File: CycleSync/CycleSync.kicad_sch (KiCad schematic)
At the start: 0 parts

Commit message: M1.1: hierarchical sheet skeleton + net-map topology (6 sheets, all interface labels placed/imported)
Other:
- added sheet Audio_ADC (Audio_ADC.kicad_sch)
- added sheet Audio_DAC (Audio_DAC.kicad_sch)
- added sheet GNSS_RF (GNSS_RF.kicad_sch)
- added sheet MCU (MCU.kicad_sch)
- added sheet Power (Power.kicad_sch)
- added sheet USB_PD (USB_PD.kicad_sch)

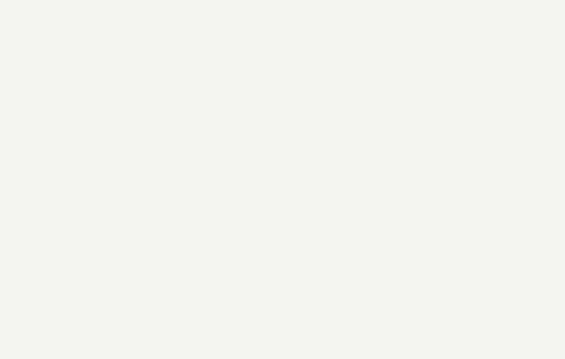
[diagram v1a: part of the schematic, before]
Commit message: M1.2: MCU core supply, fixed-function pins, GPIO0-8 assignment
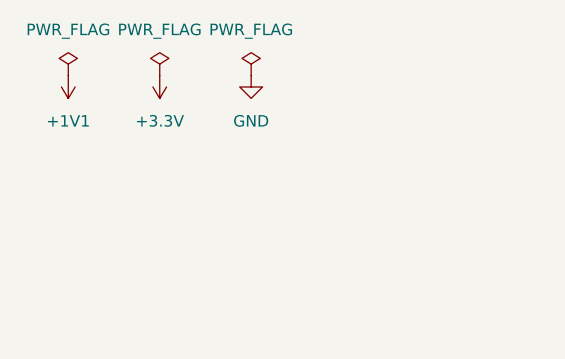
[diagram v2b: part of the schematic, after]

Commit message: finishing Phase 1.5
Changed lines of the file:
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@@
 			)
 		)
-		(pin "I2C_SCL" input
+		(pin "I2C_SCL" bidirectional
 			(at 81.6293 100.33 90)
 			(effects

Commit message: s
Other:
- added sheet Daughter_IO (Daughter_IO.kicad_sch)
- sheet Audio_ADC ports: added LINE_IN_L, LINE_IN_R; removed none
- sheet Audio_DAC ports: added LINE_OUT_L, LINE_OUT_R; removed none
- sheet GNSS_RF ports: added GNSS_BCKP_CUTOFF, GNSS_FIX_STATUS, GNSS_RESET_N; removed none
- sheet MCU ports: added GNSS_BCKP_CUTOFF, GNSS_FIX_LED, GNSS_FIX_STATUS, GNSS_RESET_N, GNSS_VCC_CUTOFF, PD_IRQ, USB_D_N, USB_D_P; removed USB_DM, USB_DP
- sheet Power ports: added GNSS_VCC_CUTOFF, PP5V, VBUS_HOST_5V, VBUS_PD_5V; removed none
- sheet USB_PD ports: added CC1, CC2, PDIN_CC1, PDIN_CC2, PD_IRQ, PP5V, PPHV, VBUS; removed USB_DM, USB_DP
- note added: "CYCLESYNC ASSEMBLY VARIANTS 1. PD + LINE-IN: PD_OPTION + LINE_IN_OPTION 2. PD + PLAYBACK-ONLY: PD_OPTION 3. NO-PD + LINE-IN: NO_PD_OPTION + LINE_IN_OPTION 4. NO-PD + PLAYBACK-ONLY: NO_PD_OPTION COMPONENTS WITH A BLANK VARIANT FIELD ARE COMMON TO ALL BUILDS UNLESS MARKED DNP."
- title: (none) -> CYCLESYNC SYSTEM SCHEMATIC

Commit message: verified schematic wirings
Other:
- sheet USB_PD ports: added VBUS_PD_5V; removed PPHV
- note added: "ASSEMBLY VARIANTS 1. PD + LINE-IN: PD_OPTION + LINE_IN_OPTION 2. PD + PLAYBACK: PD_OPTION ONLY 3. NO-PD + LINE-IN: NO_PD_OPTION + LINE_IN_OPTION 4. NO-PD + PLAYBACK: NO_PD_OPTION ONLY PD_OPTION AND NO_PD_OPTION ARE MUTUALLY EXCLUSIVE. PRIMARY FULL-FEATURE BUILD: PD + LINE-IN."
- note added: "CONFORMAL COATING, NO-COAT AREAS ALL CONNECTORS, SWITCHES, TEST POINTS, EEPROM RECOVERY PADS AND ANTENNA PADS. HAND-SOLDER ANT1 AFTER COATING."
- note added: "FIXED CONFIGURATION / ADDRESSES TPS25751 I²Ct: ADCIN1 = 0, ADCIN2 = 0 SAFEMODE, 7-BIT ADDRESS 0x21 PD EEPROM: 7-BIT ADDRESS 0x50 PCM1862: MD0 = 0, MS/AD = 0 I²C CONTROL, 7-BIT ADDRESS 0x4A LC76G: D_SEL DNP → UART INTERFACE"
- note added: "VARIANT FIELD IS ASSEMBLY DOCUMENTATION ONLY. EXPORT A SEPARATE BOM AND POSITION FILE FOR EACH ASSEMBLY VARIANT. VERIFY EVERY POPULATE/DNP LINE BEFORE RELEASE."
- note removed: "CYCLESYNC ASSEMBLY VARIANTS 1. PD + LINE-IN: PD_OPTION + LINE_IN_OPTION 2. PD + PLAYBACK-ONLY: PD_OPTION 3. NO-PD + LINE-IN: NO_PD_OPTION + LINE_IN_OPTION 4. NO-PD + PLAYBACK-ONLY: NO_PD_OPTION COMPONENTS WITH A BLANK VARIANT FIELD ARE COMMON TO ALL BUILDS UNLESS MARKED DNP."
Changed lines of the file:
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@@
 	)
 	(rectangle
-		(start 212.09 22.86)
-		(end 264.16 59.69)
+		(start 132.08 22.86)
+		(end 186.69 36.83)
 		(stroke
 			(width 0)
@@
 		)
 	)
-	(text "CYCLESYNC ASSEMBLY VARIANTS\n\n1. PD + LINE-IN:\n   PD_OPTION + LINE_IN_OPTION\n\n2. PD + PLAYBACK-ONLY:\n   PD_OPTION\n\n3. NO-PD + LINE-IN:\n   NO_PD_OPTION + LINE_IN_OPTION\n\n4. NO-PD + PLAYBACK-ONLY:\n   NO_PD_OPTION\n\nCOMPONENTS WITH A BLANK VARIANT FIELD\nARE COMMON TO ALL BUILDS UNLESS MARKED DNP."
+	(rectangle
+		(start 210.82 71.12)
+		(end 256.54 87.63)
+		(stroke
+			(width 0)
+			(type default)
+		)
+		(fill
+			(type none)
+		)
+	)
+	(rectangle
+		(start 138.43 52.07)
+		(end 176.53 86.36)
+		(stroke
+			(width 0)
+			(type default)
+		)
+		(fill
+			(type none)
+		)
+	)
+	(rectangle
+		(start 209.55 22.86)
+		(end 266.7 59.69)
+		(stroke
+			(width 0)
+			(type default)
+		)
+		(fill
+			(type none)
+		)
+	)
+	(text "ASSEMBLY VARIANTS\n\n1. PD + LINE-IN:\n   PD_OPTION + LINE_IN_OPTION\n\n2. PD + PLAYBACK:\n   PD_OPTION ONLY\n\n3. NO-PD + LINE-IN:\n   NO_PD_OPTION + LINE_IN_OPTION\n\n4. NO-PD + PLAYBACK:\n   NO_PD_OPTION ONLY\n\nPD_OPTION AND NO_PD_OPTION ARE MUTUALLY EXCLUSIVE.\nPRIMARY FULL-FEATURE BUILD: PD + LINE-IN."
 		(exclude_from_sim no)
 		(at 238.252 41.148 0)
+		(effects
+			(font
+				(size 1.27 1.27)
+			)
+		)
+	)
+	(text "CONFORMAL COATING, NO-COAT AREAS\n\nALL CONNECTORS, SWITCHES, TEST POINTS,\nEEPROM RECOVERY PADS AND ANTENNA PADS.\n\nHAND-SOLDER ANT1 AFTER COATING."
+		(exclude_from_sim no)
+		(at 233.68 80.264 0)
+		(effects
+			(font
+				(size 1.27 1.27)
+			)
+		)
+	)
+	(text "FIXED CONFIGURATION / ADDRESSES\n\nTPS25751 I²Ct:\nADCIN1 = 0, ADCIN2 = 0\nSAFEMODE, 7-BIT ADDRESS 0x21\n\nPD EEPROM: 7-BIT ADDRESS 0x50\n\nPCM1862:\nMD0 = 0, MS/AD = 0\nI²C CONTROL, 7-BIT ADDRESS 0x4A\n\nLC76G:\nD_SEL DNP → UART INTERFACE"
+		(exclude_from_sim no)
+		(at 157.734 69.596 0)
+		(effects
+			(font
+				(size 1.27 1.27)
+			)
+		)
+	)
+	(text "VARIANT FIELD IS ASSEMBLY DOCUMENTATION ONLY.\n\nEXPORT A SEPARATE BOM AND POSITION FILE\nFOR EACH ASSEMBLY VARIANT.\nVERIFY EVERY POPULATE/DNP LINE BEFORE RELEASE."
+		(exclude_from_sim no)
+		(at 157.988 29.464 0)
 		(effects
 			(font
@@
 			)
 		)
-		(pin "PPHV" bidirectional
+		(pin "VBUS_PD_5V" bidirectional
 			(at 33.02 44.45 0)
 			(effects

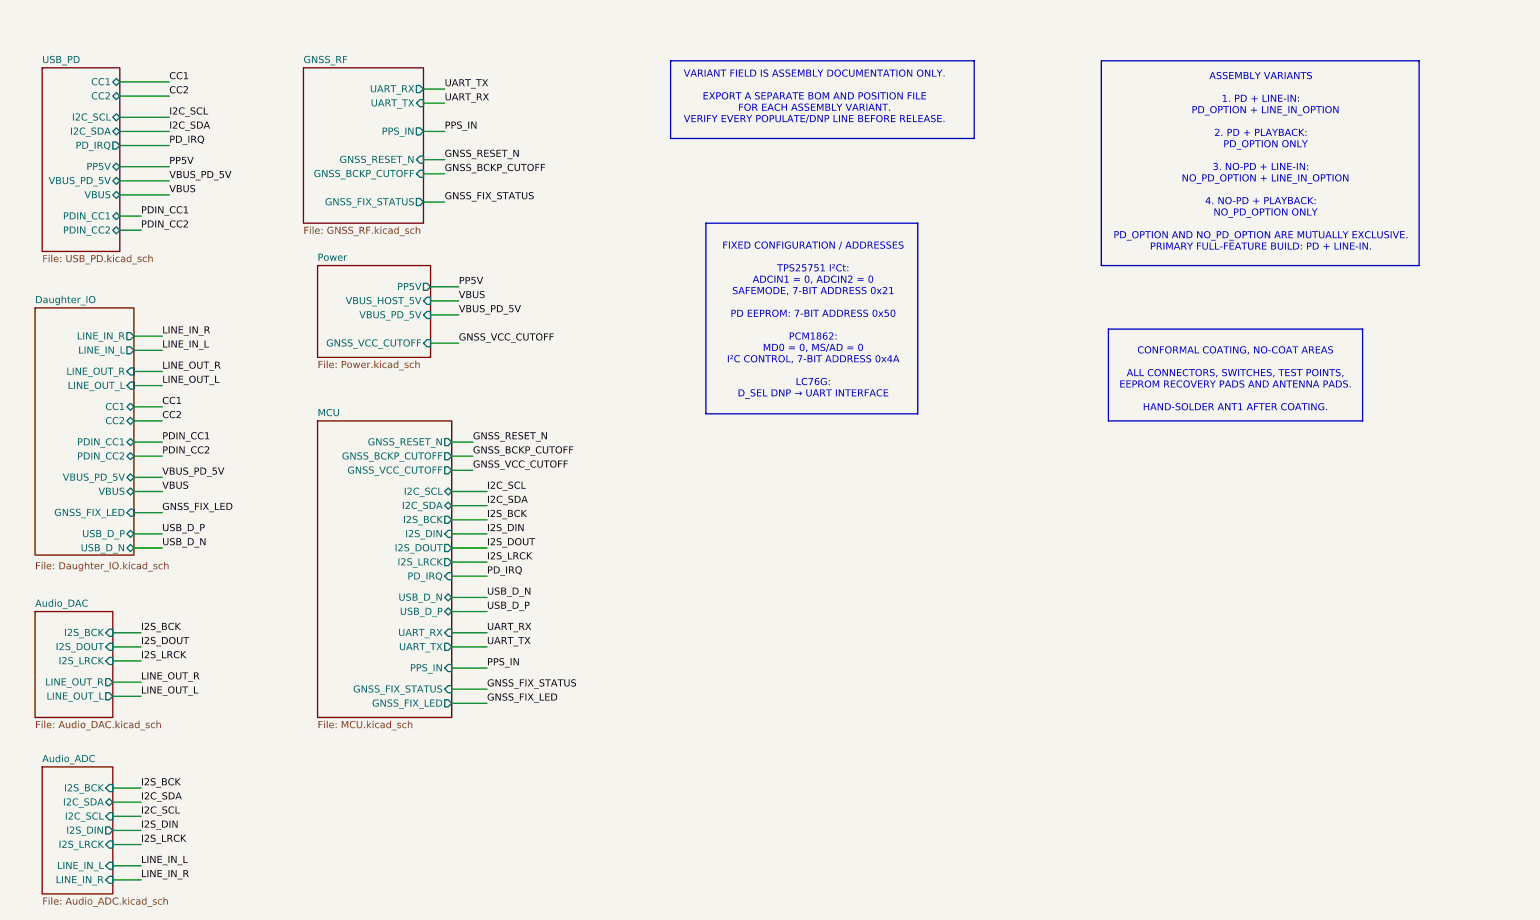
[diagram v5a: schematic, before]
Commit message: added footprints and manufacturer part number
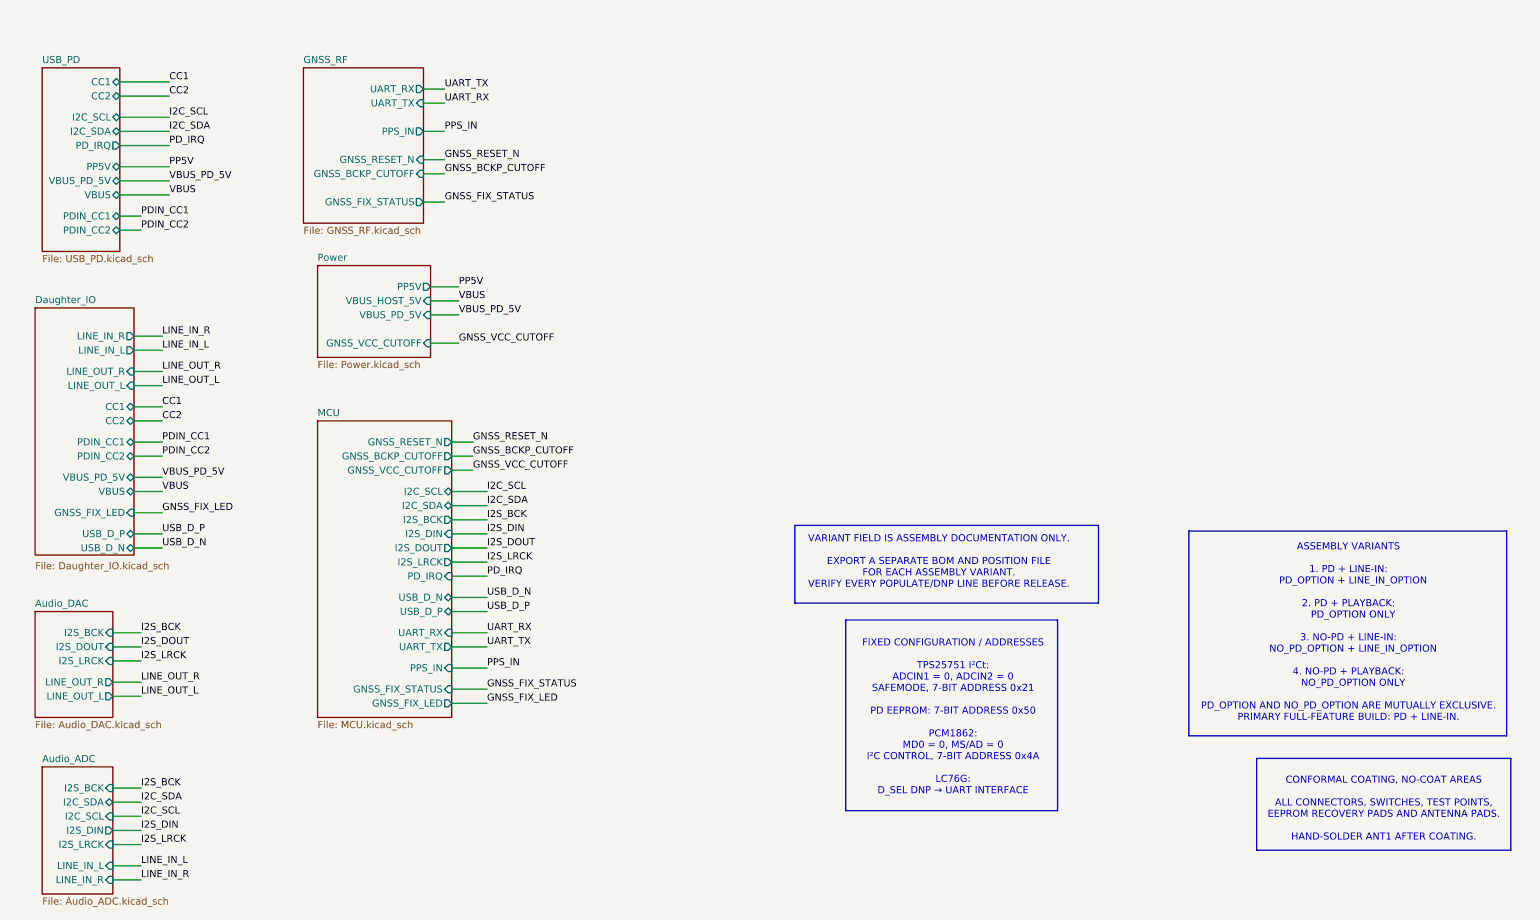
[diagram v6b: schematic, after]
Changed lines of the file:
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@@
 	)
 	(rectangle
-		(start 132.08 22.86)
-		(end 186.69 36.83)
+		(start 154.432 106.426)
+		(end 209.042 120.396)
 		(stroke
 			(width 0)
@@
 	)
 	(rectangle
-		(start 210.82 71.12)
-		(end 256.54 87.63)
+		(start 237.49 148.336)
+		(end 283.21 164.846)
 		(stroke
 			(width 0)
@@
 	)
 	(rectangle
-		(start 138.43 52.07)
-		(end 176.53 86.36)
+		(start 163.576 123.444)
+		(end 201.676 157.734)
 		(stroke
 			(width 0)
@@
 	)
 	(rectangle
-		(start 209.55 22.86)
-		(end 266.7 59.69)
+		(start 225.298 107.442)
+		(end 282.448 144.272)
 		(stroke
 			(width 0)
@@
 	(text "ASSEMBLY VARIANTS\n\n1. PD + LINE-IN:\n   PD_OPTION + LINE_IN_OPTION\n\n2. PD + PLAYBACK:\n   PD_OPTION ONLY\n\n3. NO-PD + LINE-IN:\n   NO_PD_OPTION + LINE_IN_OPTION\n\n4. NO-PD + PLAYBACK:\n   NO_PD_OPTION ONLY\n\nPD_OPTION AND NO_PD_OPTION ARE MUTUALLY EXCLUSIVE.\nPRIMARY FULL-FEATURE BUILD: PD + LINE-IN."
 		(exclude_from_sim no)
-		(at 238.252 41.148 0)
+		(at 254 125.73 0)
 		(effects
 			(font
@@
 	(text "CONFORMAL COATING, NO-COAT AREAS\n\nALL CONNECTORS, SWITCHES, TEST POINTS,\nEEPROM RECOVERY PADS AND ANTENNA PADS.\n\nHAND-SOLDER ANT1 AFTER COATING."
 		(exclude_from_sim no)
-		(at 233.68 80.264 0)
+		(at 260.35 157.48 0)
 		(effects
 			(font
@@
 	(text "FIXED CONFIGURATION / ADDRESSES\n\nTPS25751 I²Ct:\nADCIN1 = 0, ADCIN2 = 0\nSAFEMODE, 7-BIT ADDRESS 0x21\n\nPD EEPROM: 7-BIT ADDRESS 0x50\n\nPCM1862:\nMD0 = 0, MS/AD = 0\nI²C CONTROL, 7-BIT ADDRESS 0x4A\n\nLC76G:\nD_SEL DNP → UART INTERFACE"
 		(exclude_from_sim no)
-		(at 157.734 69.596 0)
+		(at 182.88 140.97 0)
 		(effects
 			(font
@@
 	(text "VARIANT FIELD IS ASSEMBLY DOCUMENTATION ONLY.\n\nEXPORT A SEPARATE BOM AND POSITION FILE\nFOR EACH ASSEMBLY VARIANT.\nVERIFY EVERY POPULATE/DNP LINE BEFORE RELEASE."
 		(exclude_from_sim no)
-		(at 157.988 29.464 0)
+		(at 180.34 113.03 0)
 		(effects
 			(font
